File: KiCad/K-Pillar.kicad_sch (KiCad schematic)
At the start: 6 parts, among them J1 I2COut, J2 Kaypad, M1 Motor_DC, Q1 IRLZ34N, U1 ATmega328-P, U2 L7805

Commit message: płytka zrobiona można na narty
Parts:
- removed J2: Kaypad, symbol Connector:Conn_01x08_Socket
- removed U1: ATmega328-P, Package_DIP:DIP-28_W7.62mm, symbol MCU_Microchip_ATmega:ATmega328-P
- removed U2: L7805, symbol Regulator_Linear:L7805
- added 12V1, 5V1: Conn_01x02_Pin, Connector_PinHeader_2.54mm:PinHeader_1x02_P2.54mm_Vertical, symbol Connector:Conn_01x02_Pin
- added A1: Arduino_Nano_v3.x, Module:Arduino_Nano, symbol MCU_Module:Arduino_Nano_v3.x
- added C1: 100n, Capacitor_SMD:C_0805_2012Metric_Pad1.18x1.45mm_HandSolder, symbol Device:C
- added C2: 100u, Capacitor_THT:CP_Radial_D5.0mm_P2.50mm, symbol Device:C_Polarized
- added J2: Keypad, Connector_PinHeader_2.54mm:PinHeader_1x07_P2.54mm_Vertical, symbol Connector:Conn_01x07_Pin
- added J3: Relay, Connector_PinHeader_2.54mm:PinHeader_1x03_P2.54mm_Vertical, symbol Connector:Conn_01x03_Pin
- added M2, M3: Pump, TerminalBlock_4Ucon:TerminalBlock_4Ucon_1x02_P3.50mm_Horizontal, symbol Motor:Motor_DC
- added Q2, Q3: IRLZ44N, Package_TO_SOT_THT:TO-220-3_Vertical, symbol Transistor_FET:IRLZ34N
- J1: footprint (none) -> Connector_PinHeader_2.54mm:PinHeader_1x04_P2.54mm_Vertical
- M1: value Motor_DC -> Pump; footprint (none) -> TerminalBlock_4Ucon:TerminalBlock_4Ucon_1x02_P3.50mm_Horizontal
- Q1: value IRLZ34N -> IRLZ44N
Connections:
- net GND: now reaches J1.1 (Pin_1)
- net GND: now also Q1.3 (S), 12V1.2 (Pin_2), 5V1.2 (Pin_2), A1.29 (GND), A1.4 (GND), C1.1, C2.2, J3.1 (Pin_1), Q2.3 (S), Q3.3 (S)
- net +5V: now reaches J1.2 (Pin_2)
- net +5V: now also 5V1.1 (Pin_1), A1.27 (+5V), C1.2, C2.1, J3.2 (Pin_2)
- net at J1.3 (Pin_3): now also A1.23 (A4)
- net at J1.4 (Pin_4): now also A1.24 (A5)
- net +12V: now reaches M1.1 (+)
- net +12V: now also 12V1.1 (Pin_1), M2.1 (+), M3.1 (+)
- net at M1.2 (-): now also Q1.2 (D)
- net PUMP1: now reaches Q1.1 (G)
- net PUMP1: now also A1.19 (A0)
- new net: M3.2 (-), Q3.2 (D)
- new net: A1.10 (D7), J2.6 (Pin_6)
- new net: A1.11 (D8), J2.7 (Pin_7)
- new net: A1.22 (A3), J3.3 (Pin_3)
- new net: A1.5 (D2), J2.1 (Pin_1)
- new net: A1.6 (D3), J2.2 (Pin_2)
- new net: A1.7 (D4), J2.3 (Pin_3)
- new net: A1.8 (D5), J2.4 (Pin_4)
- new net: A1.9 (D6), J2.5 (Pin_5)
- new net: M2.2 (-), Q2.2 (D)
- new net PUMP2: A1.20 (A1), Q2.1 (G)
- new net PUMP3: A1.21 (A2), Q3.1 (G)
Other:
- moved on the sheet: J1, M1, Q1

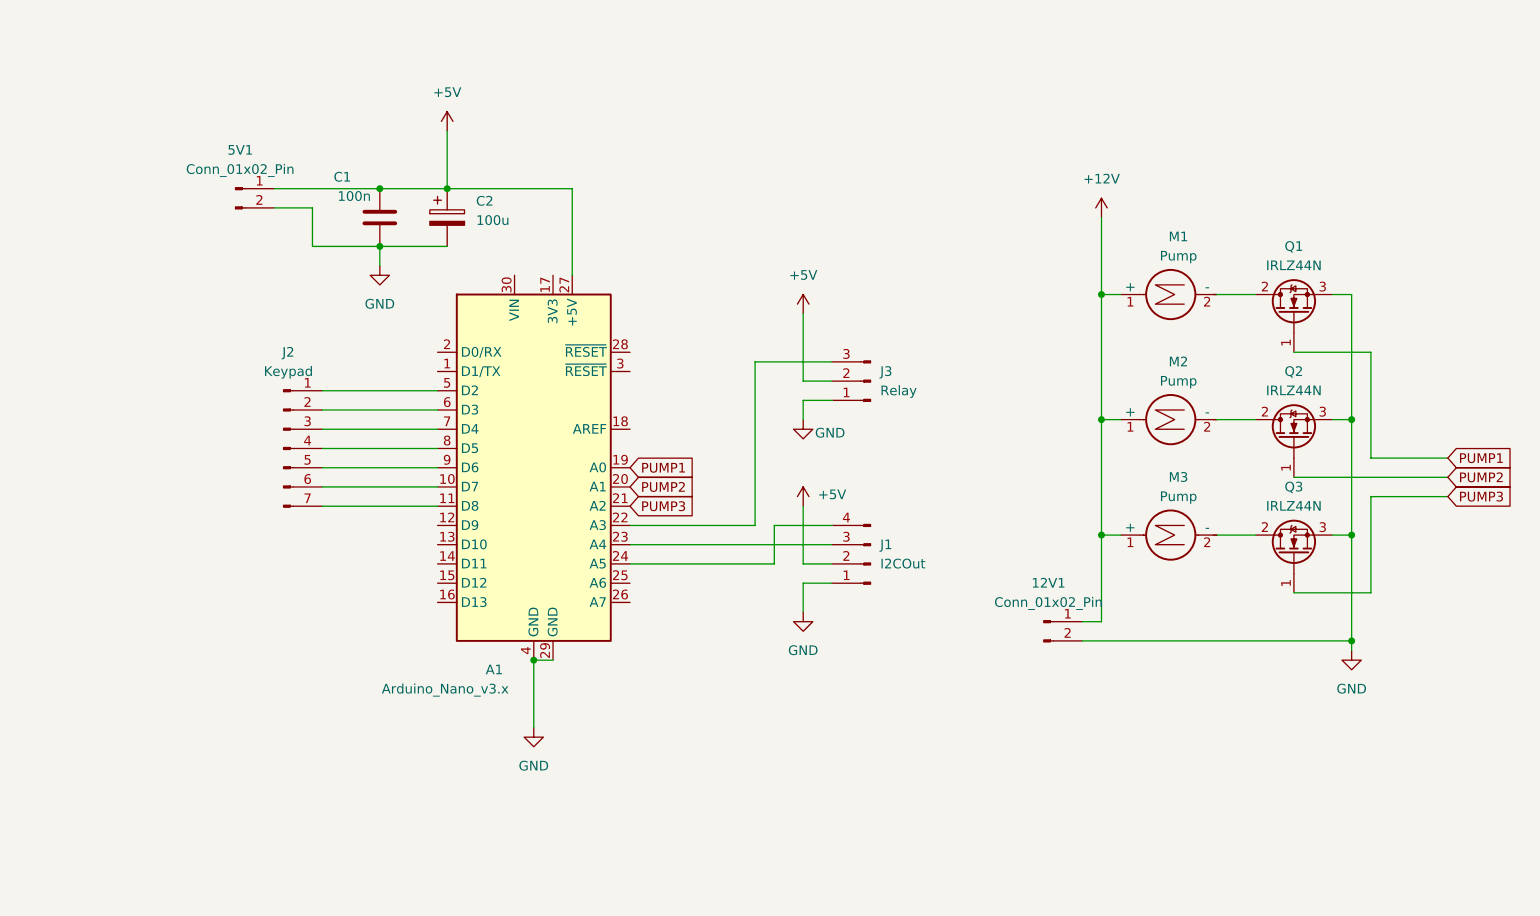
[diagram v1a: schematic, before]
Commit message: started working on v2 board
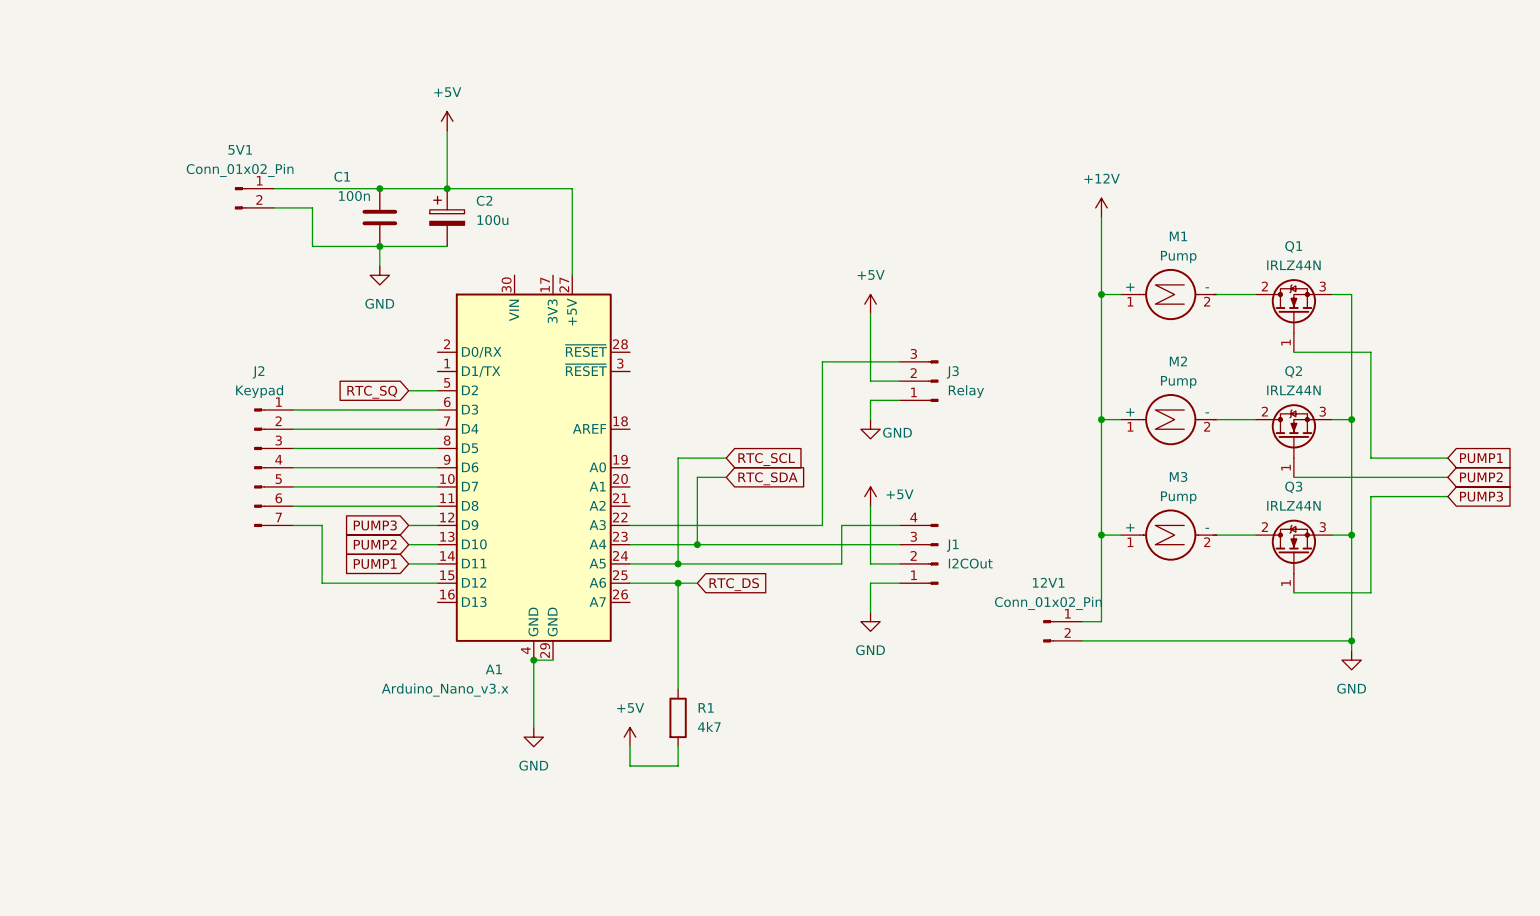
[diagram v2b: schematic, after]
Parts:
- added R1: 4k7, symbol Device:R
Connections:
- net +5V: now also R1.2
- net PUMP1: now also A1.14 (D11); no longer A1.19 (A0)
- net PUMP2: now also A1.13 (D10); no longer A1.20 (A1)
- net PUMP3: now also A1.12 (D9); no longer A1.21 (A2)
- net at A1.10 (D7): now also J2.5 (Pin_5); no longer J2.6 (Pin_6)
- net at A1.11 (D8): now also J2.6 (Pin_6); no longer J2.7 (Pin_7)
- net at A1.15 (D12): now also J2.7 (Pin_7)
- net RTC_SDA: now reaches A1.23 (A4), J1.3 (Pin_3)
- net RTC_SCL: now reaches A1.24 (A5), J1.4 (Pin_4)
- net RTC_DS: now reaches A1.25 (A6)
- net RTC_DS: now also R1.1
- net at J2.1 (Pin_1): now also A1.6 (D3); no longer A1.5 (D2)
- net at J2.2 (Pin_2): now also A1.7 (D4); no longer A1.6 (D3)
- net at J2.3 (Pin_3): now also A1.8 (D5); no longer A1.7 (D4)
- net at J2.4 (Pin_4): now also A1.9 (D6); no longer A1.8 (D5)
- new net RTC_SQ: A1.5 (D2)
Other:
- moved on the sheet: J1, J2, J3

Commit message: board v2
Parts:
- added J4: RTC, Connector_PinHeader_2.54mm:PinHeader_1x07_P2.54mm_Vertical, symbol Connector:Conn_01x07_Pin
- added R2: 10k, Resistor_SMD:R_0805_2012Metric_Pad1.20x1.40mm_HandSolder, symbol Device:R
- R1: footprint (none) -> Resistor_SMD:R_0805_2012Metric_Pad1.20x1.40mm_HandSolder
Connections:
- net +5V: now also J4.3 (Pin_3)
- net GND: now also J4.2 (Pin_2)
- net RTC_DS: now also J4.6 (Pin_6)
- net RTC_SCL: now also J4.5 (Pin_5)
- net RTC_SDA: now also J4.4 (Pin_4)
- net RTC_SQ: now also J4.7 (Pin_7)
- net at A1.17 (3V3): now also R2.2
- net at A1.18 (AREF): now also R2.1
- net RTC_BAT: now reaches A1.26 (A7)
- net RTC_BAT: now also J4.1 (Pin_1)
